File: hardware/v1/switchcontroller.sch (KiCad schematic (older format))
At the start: 1 part, among them U3 MCP23017

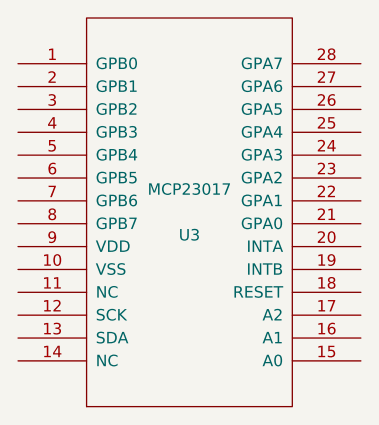
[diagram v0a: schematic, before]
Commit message: Add new schematics for additional switch boards
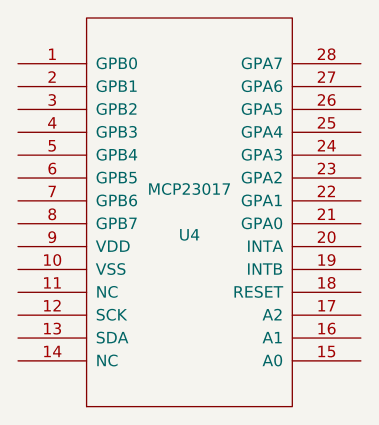
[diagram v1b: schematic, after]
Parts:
- renumbered U3 to U4
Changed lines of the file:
@@
 $Descr A4 11693 8268
 encoding utf-8
-Sheet 8 27
+Sheet 8 30
 Title ""
 Date ""
@@
 $EndDescr
 $Comp
-L MCP23017 U3
+L MCP23017 U4
 U 1 1 57A3D3D3
 P 4900 3000
-F 0 "U3" H 4900 2900 50  0000 C CNN
+F 0 "U4" H 4900 2900 50  0000 C CNN
 F 1 "MCP23017" H 4900 3100 50  0000 C CNN
 F 2 "DIL28:DIL28" H 4900 3000 50  0001 C CNN
